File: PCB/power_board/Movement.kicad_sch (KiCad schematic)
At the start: 3 parts, among them IC10 LSM6DSV16BXTR, J9 QVAR

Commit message: everything before jlc template
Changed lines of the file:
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@@
 	)
 	(hierarchical_label "VOUT_3V3"
-		(shape input)
+		(shape output)
 		(at 77.47 43.18 90)
 		(effects
@@
 	)
 	(hierarchical_label "VOUT_3V3"
-		(shape input)
+		(shape output)
 		(at 43.18 71.12 180)
 		(effects
@@
 	)
 	(hierarchical_label "VOUT_3V3"
-		(shape input)
+		(shape output)
 		(at 187.96 104.14 270)
 		(effects
@@
 	)
 	(hierarchical_label "VOUT_3V3"
-		(shape input)
+		(shape output)
 		(at 218.44 77.47 0)
 		(effects

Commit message: all my pcb
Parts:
- removed J9: QVAR, Connector_JST:JST_PH_B3B-PH-K_1x03_P2.00mm_Vertical, symbol Connector_Generic:Conn_01x03
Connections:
- no-connect marks 2 -> 4

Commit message: imu from board
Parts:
- removed IC10: LSM6DSV16BXTR, LSM6DSV16BXTR:LSM6DSV16BXTR, symbol LSM6DSV16BXTR:LSM6DSV16BXTR
- added J4: IMU_connector, Connector_PinHeader_2.54mm:PinHeader_2x05_P2.54mm_Vertical, symbol Connector_Generic:Conn_02x05_Odd_Even
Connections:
- net GND: now also J4.2 (Pin_2)
- net IMU_CS: now also J4.9 (Pin_9)
- net IMU_INT1: now also J4.8 (Pin_8)
- net IMU_INT2: now also J4.10 (Pin_10)
- net MISO: now also J4.3 (Pin_3)
- net MOSI: now also J4.5 (Pin_5)
- net SCLK: now also J4.7 (Pin_7)
- net VOUT_3V3: now also J4.1 (Pin_1)
- new net SCX: J4.6 (Pin_6)
- new net SDX: J4.4 (Pin_4)
- no-connect marks 4 -> 2

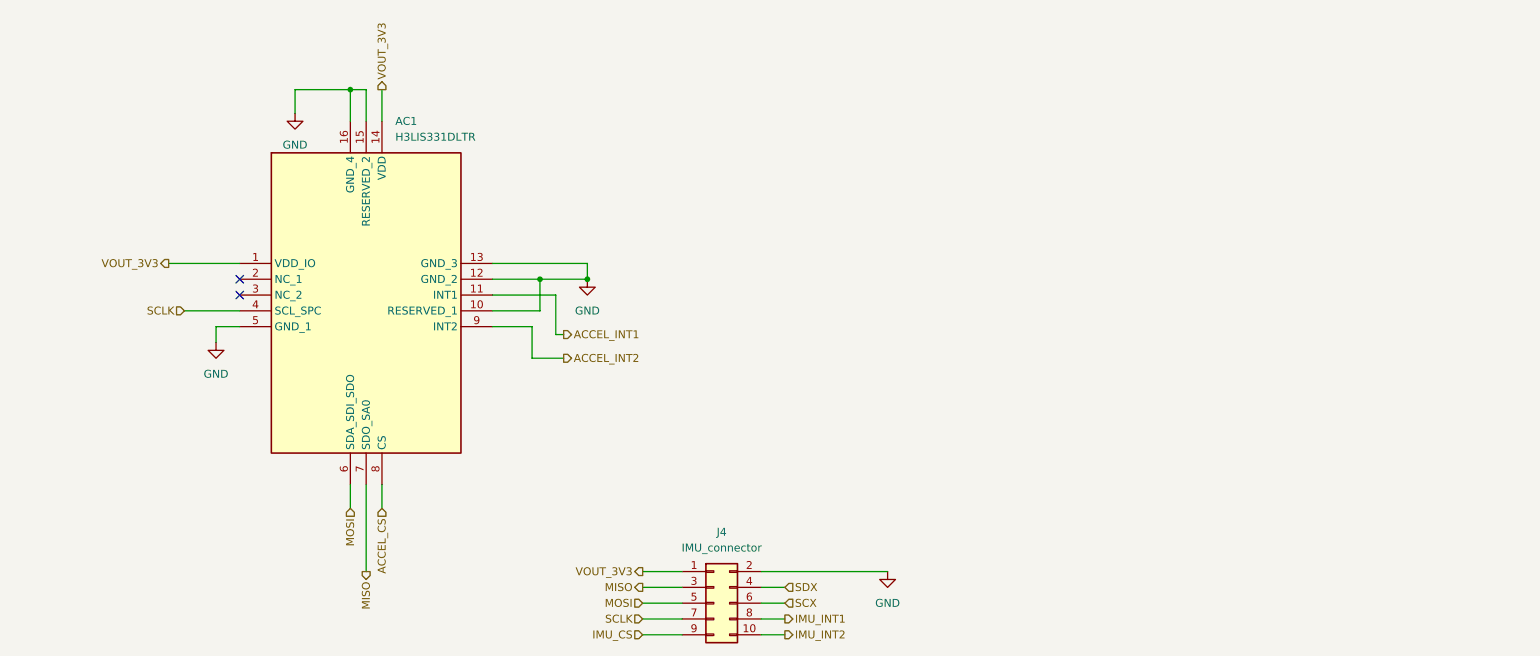
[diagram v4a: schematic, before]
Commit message: accel changed to goldpin
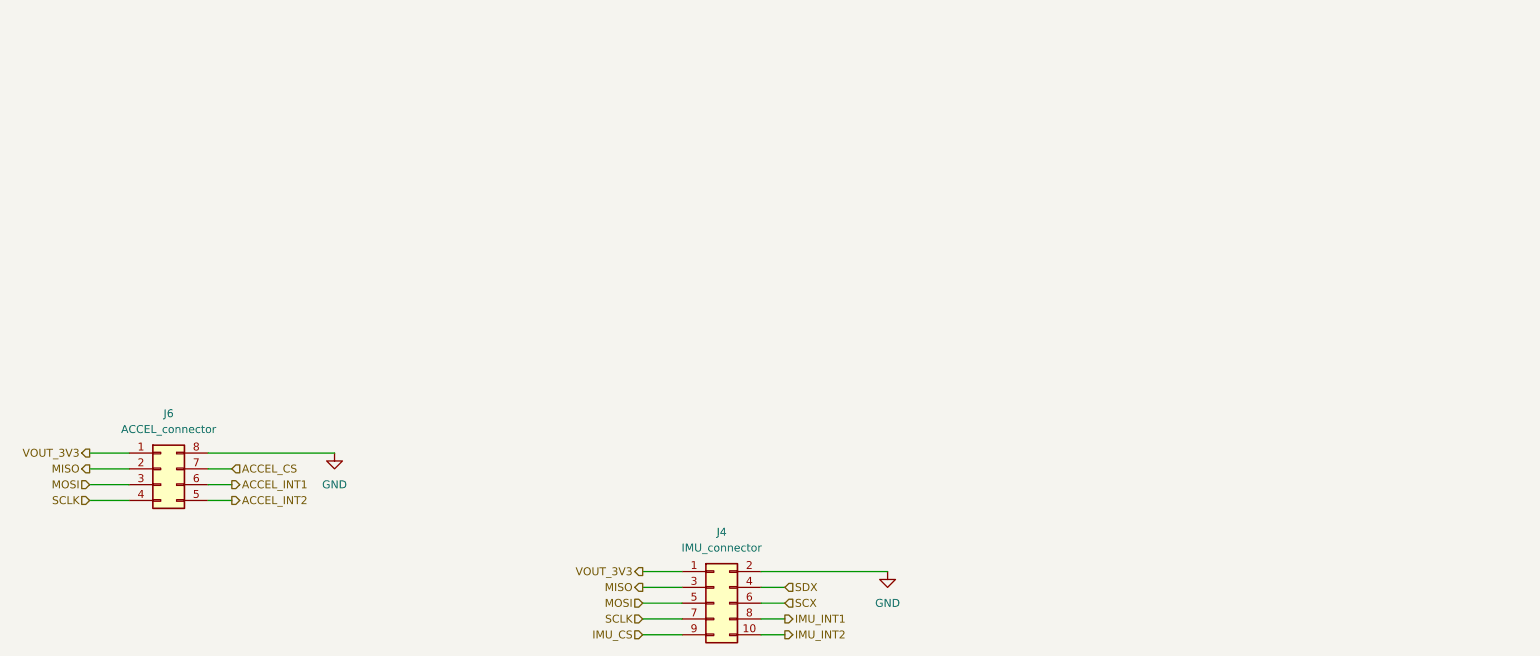
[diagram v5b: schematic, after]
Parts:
- removed AC1: H3LIS331DLTR, H3LIS331DLTR:LIS3DHTR, symbol H3LIS331DLTR:H3LIS331DLTR
- added J6: ACCEL_connector, Connector_PinHeader_2.54mm:PinHeader_2x04_P2.54mm_Vertical, symbol Connector_Generic:Conn_02x04_Counter_Clockwise
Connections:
- net ACCEL_CS: now also J6.7 (Pin_7)
- net ACCEL_INT1: now also J6.6 (Pin_6)
- net ACCEL_INT2: now also J6.5 (Pin_5)
- net GND: now also J6.8 (Pin_8)
- net MISO: now also J6.2 (Pin_2)
- net MOSI: now also J6.3 (Pin_3)
- net SCLK: now also J6.4 (Pin_4)
- net VOUT_3V3: now also J6.1 (Pin_1)
- no-connect marks 2 -> 0
